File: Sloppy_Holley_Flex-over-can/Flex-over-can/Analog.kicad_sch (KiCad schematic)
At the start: 19 parts, among them U10 ADS1115IDGSR

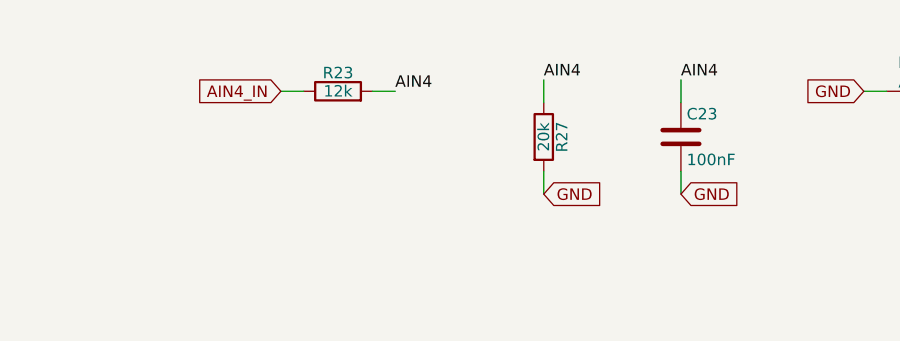
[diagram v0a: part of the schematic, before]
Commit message: Add PCB placement notes for decoupling caps to each sheet
Co-Authored-By: Claude Opus 5.5 <noreply@anthropic.com>
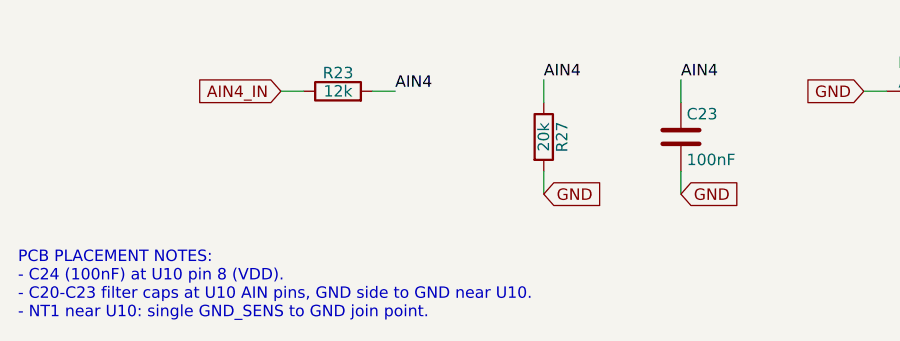
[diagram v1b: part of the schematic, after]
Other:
- note added: "PCB PLACEMENT NOTES: - C24 (100nF) at U10 pin 8 (VDD). - C20-C23 filter caps at U10 AIN pins, GND side to GND near U10. - NT1 near U10: single GND_SENS to GND join point."
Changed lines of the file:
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@@
 		)
 	)
+  (text "PCB PLACEMENT NOTES:\n- C24 (100nF) at U10 pin 8 (VDD).\n- C20-C23 filter caps at U10 AIN pins, GND side to GND near U10.\n- NT1 near U10: single GND_SENS to GND join point."
+    (at 15.24 180.34 0)
+    (effects (font (size 1.27 1.27) (color 0 0 194 1)) (justify left bottom))
+  )
 	(symbol
 		(lib_id "Device:C")
